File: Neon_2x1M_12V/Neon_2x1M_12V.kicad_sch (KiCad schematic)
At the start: 48 parts, among them J1 Conn_01x16_Pin, J2 Barrel_Jack_MountingPin, J3 Conn_01x16_Pin, J4 Barrel_Jack_MountingPin, J5 Barrel_Jack_MountingPin, J6 Conn_01x03_Pin, Q1 IRLML2502TRPBF, Q2 IRLML2502TRPBF, Q3 BSS138, Q4 BSS138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

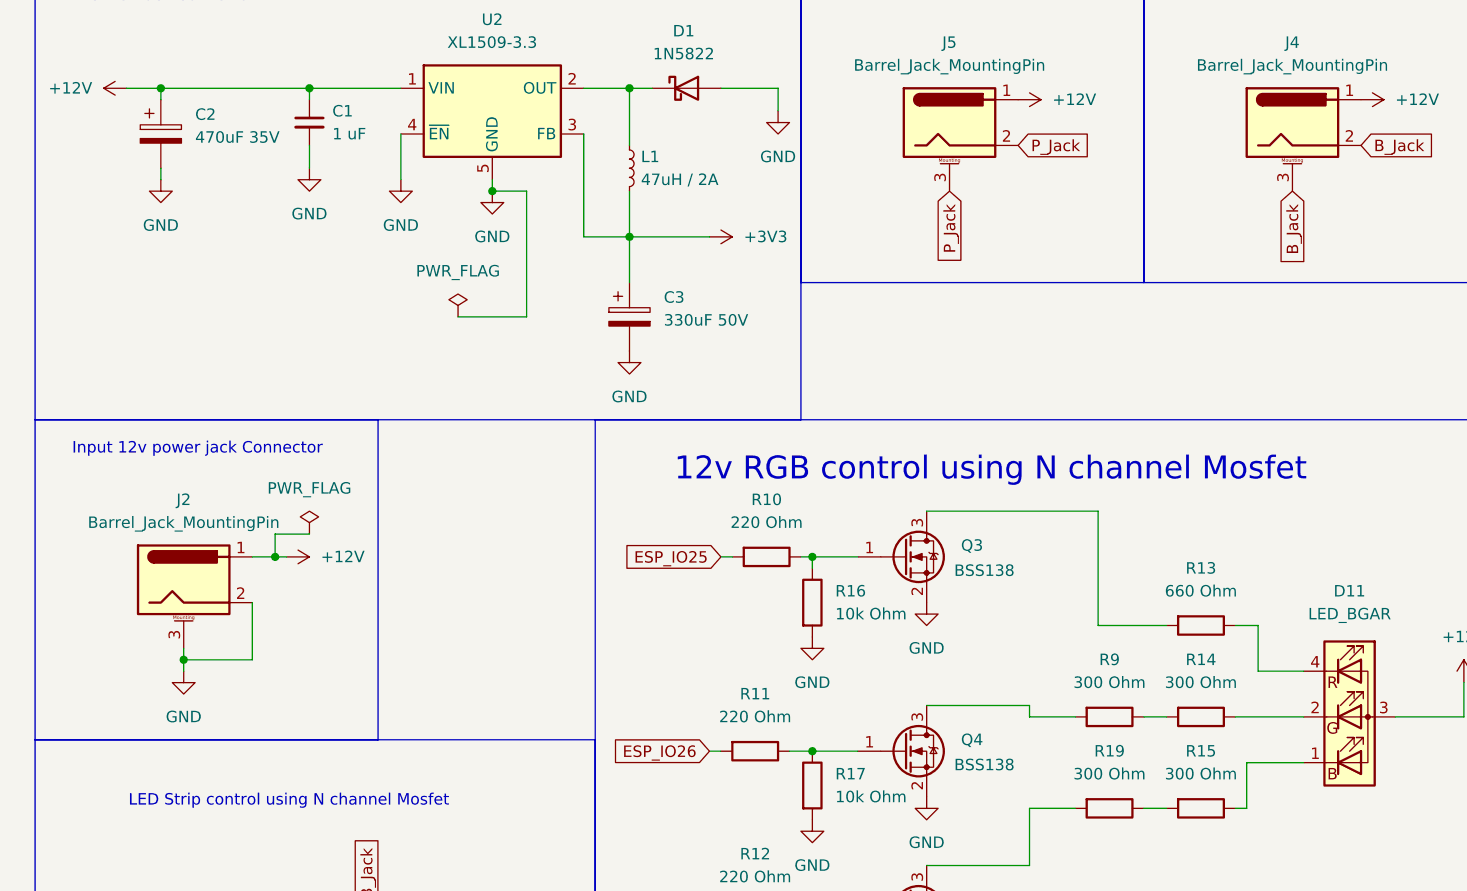
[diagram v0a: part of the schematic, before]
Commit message: updated switching pin (3) the mounting pin to be unconnected as it is not important
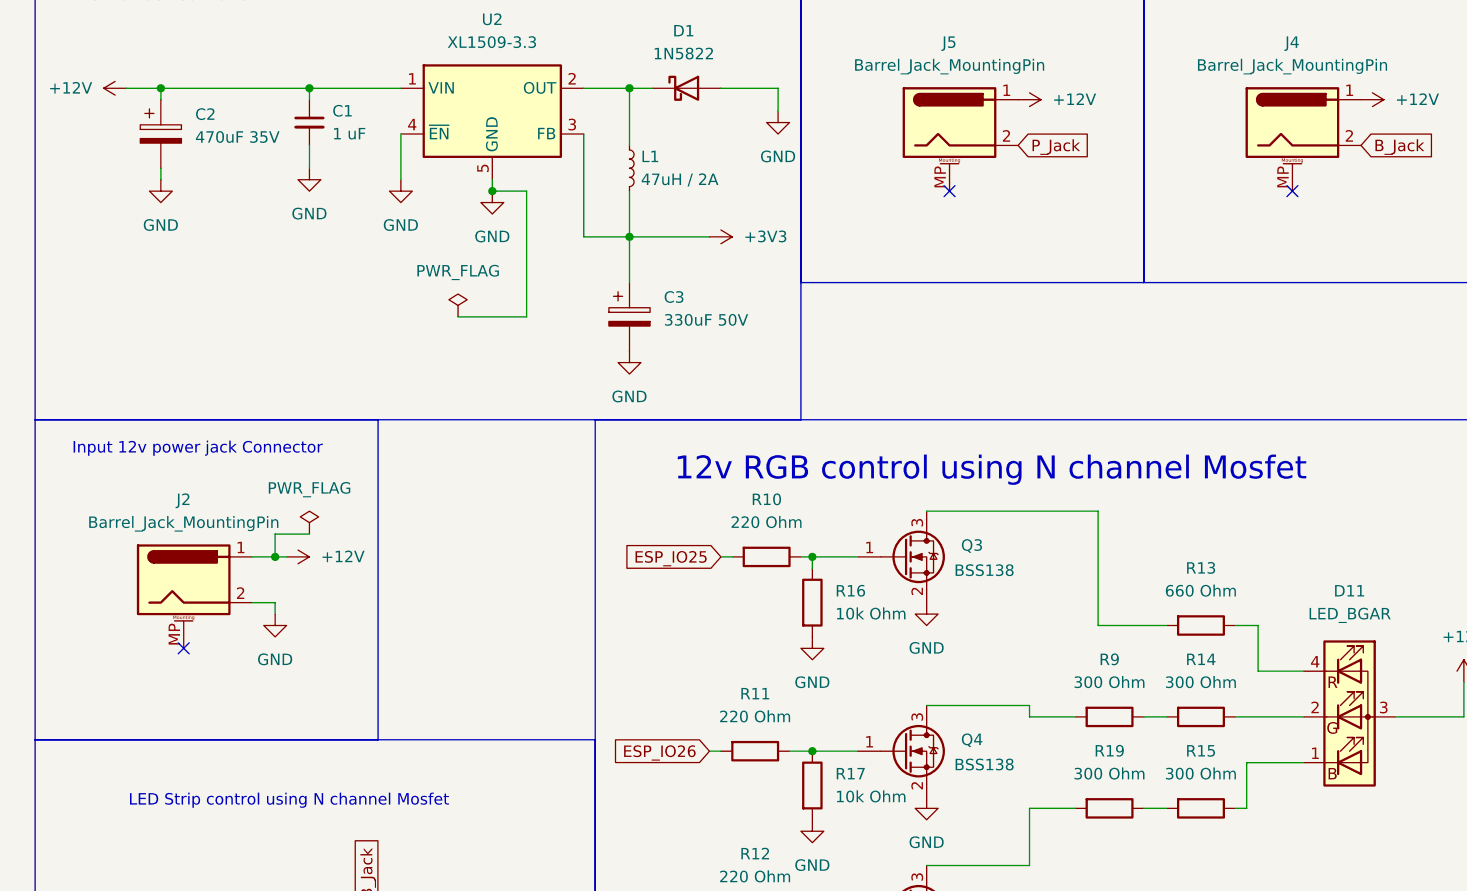
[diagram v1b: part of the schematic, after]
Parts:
- J2, J4, J5: footprint Connector_BarrelJack:BarrelJack_Horizontal -> (none); link https://makerselectronics.com/product/dc-power-jack-female-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 -> (none)
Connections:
- net B_Jack: no longer J4.3 (MountPin)
- net GND: no longer J2.3 (MountPin)
- net P_Jack: no longer J5.3 (MountPin)
- no-connect marks 6 -> 9

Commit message: generated BOM
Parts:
- J2, J4, J5: footprint (none) -> Connector_BarrelJack:BarrelJack_Horizontal
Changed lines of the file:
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@@
 	)
 	(symbol
+		(lib_name "Barrel_Jack_MountingPin_1")
 		(lib_id "Connector:Barrel_Jack_MountingPin")
 		(at 114.3 30.48 0)
@@
 			)
 		)
-		(property "Footprint" ""
+		(property "Footprint" "Connector_BarrelJack:BarrelJack_Horizontal"
 			(at 115.57 31.496 0)
 			(effects
@@
 		(pin "1"
 		)
-		(pin "MP"
+		(pin "3"
 		)
 		(pin "2"
@@
 	)
 	(symbol
+		(lib_name "Barrel_Jack_MountingPin_2")
 		(lib_id "Connector:Barrel_Jack_MountingPin")
 		(at 152.4 30.48 0)
@@
 			)
 		)
-		(property "Footprint" ""
+		(property "Footprint" "Connector_BarrelJack:BarrelJack_Horizontal"
 			(at 153.67 31.496 0)
 			(effects
@@
 		(pin "1"
 		)
-		(pin "MP"
+		(pin "3"
 		)
 		(pin "2"
@@
 			)
 		)
-		(property "Footprint" ""
+		(property "Footprint" "Connector_BarrelJack:BarrelJack_Horizontal"
 			(at 30.48 82.296 0)
 			(effects
@@
 		(pin "1"
 		)
-		(pin "MP"
+		(pin "3"
 		)
 		(pin "2"
